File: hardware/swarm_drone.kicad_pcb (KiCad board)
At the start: 4 copper layers, 45 x 45 mm, 105 parts, among them J1 Conn_01x02_Pin, J2 Conn_01x03_Socket, J3 Conn_01x03_Socket, J5 Conn_01x02_Socket, J6 Conn_01x02_Socket, J7 Conn_01x02_Socket, J8 Conn_01x02_Socket, Q1 AO3400A, Q2 AO3400A, Q3 AO3400A, Q4 AO3400A, SW1 SW_Push, U1 STM32F405RGT7, U2 TPS7A91, U3 ICM-42688-P, U4 BMP581, U5 VL53L1CXV0FY1, U6 GD25Q128ESIGR, U7 nRF24L01P, X1 8MHz, Y1 16MHz (C13738)

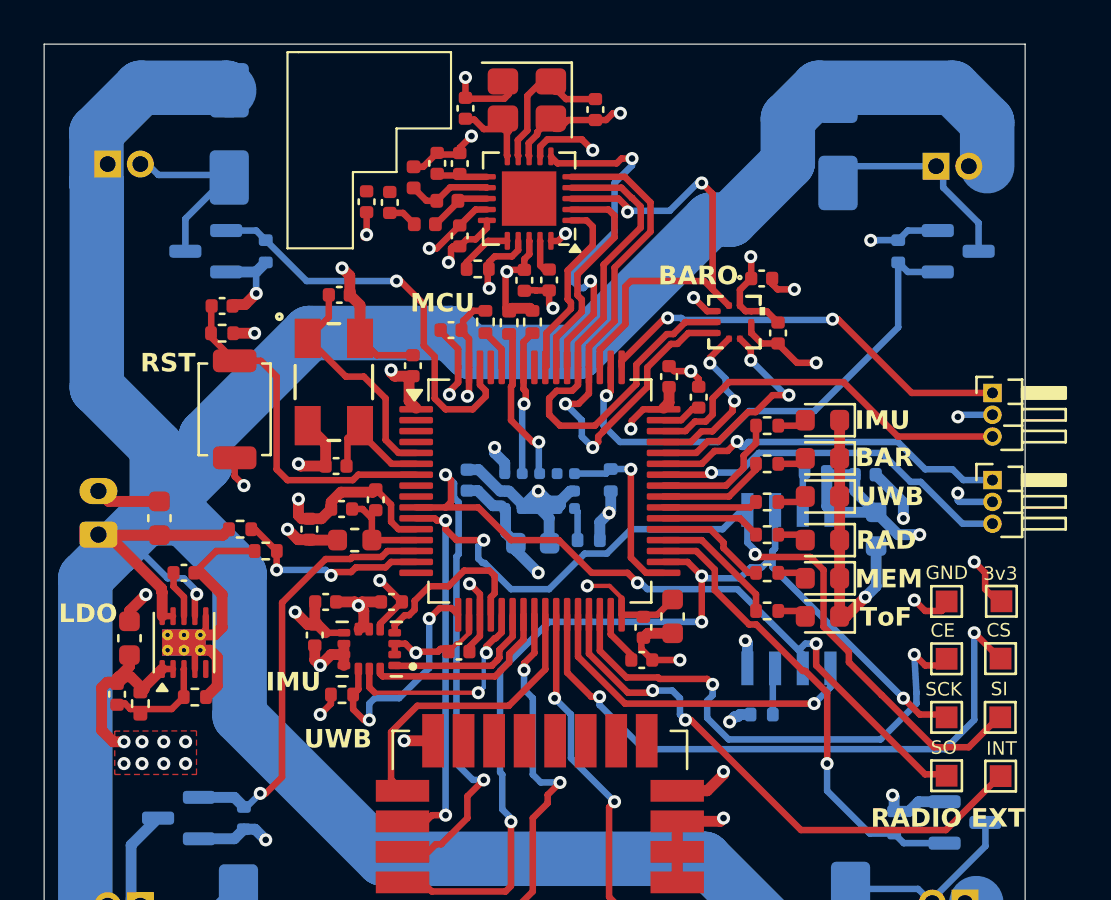
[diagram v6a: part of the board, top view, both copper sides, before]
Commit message: feat(kicad): Added chip antenna footprint Still deciding between chip vs trace
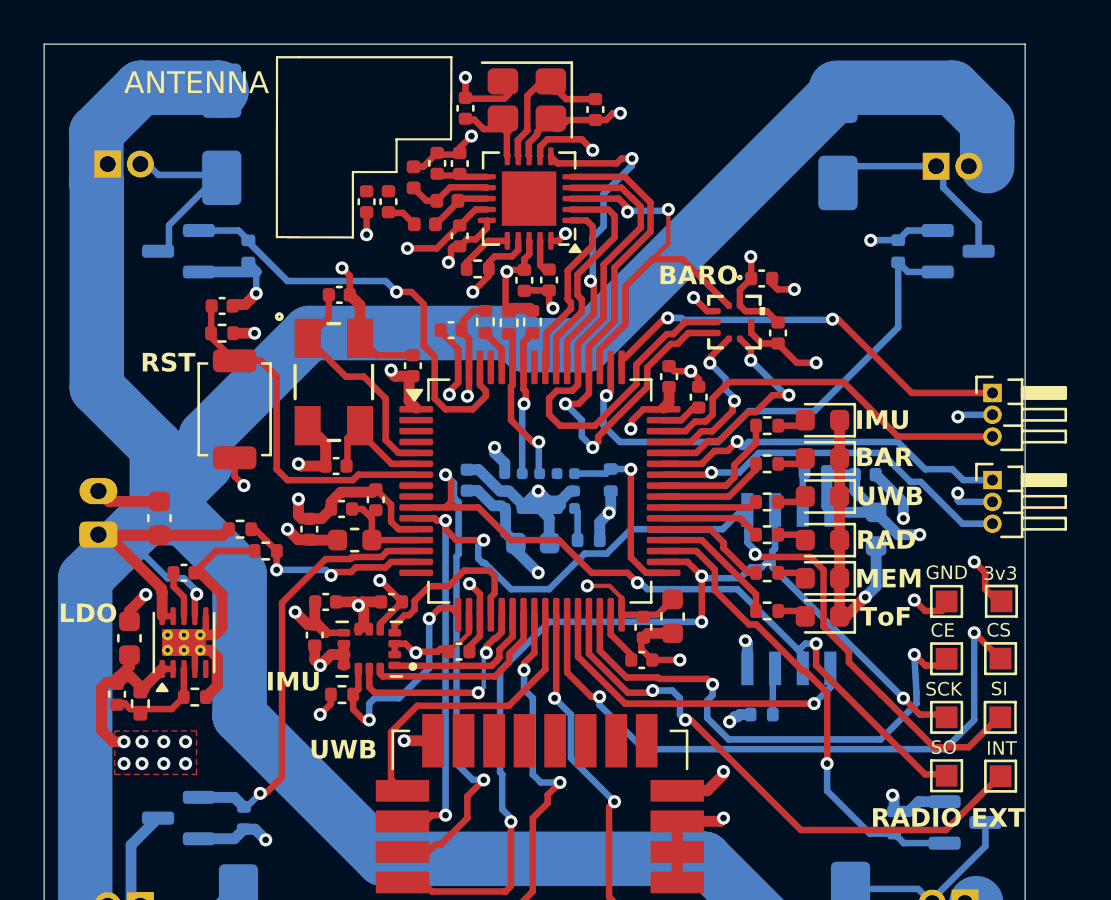
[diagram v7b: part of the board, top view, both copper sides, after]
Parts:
- moved Q1 1.25 mm to (84.5, 49.1)
- moved R12 0.80 mm to (87.7, 49.1)
- moved D1 0.34 mm to (86.5, 43.8)
- moved C33 0.07 mm to (94.1, 46.9)
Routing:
- net /Barometer/SPI3_SCK: track 21.5 -> 17.8 mm
- net GND: track 153.6 -> 155.7 mm
- net +BATT: track 177.0 -> 175.2 mm
- net /Microcontroller/RADIO_INT: track 16.3 -> 14.9 mm
- net /Microcontroller/M1: track 19.2 -> 20.0 mm
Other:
- board text added: "ANTENNA"
- board text removed: "MCU"

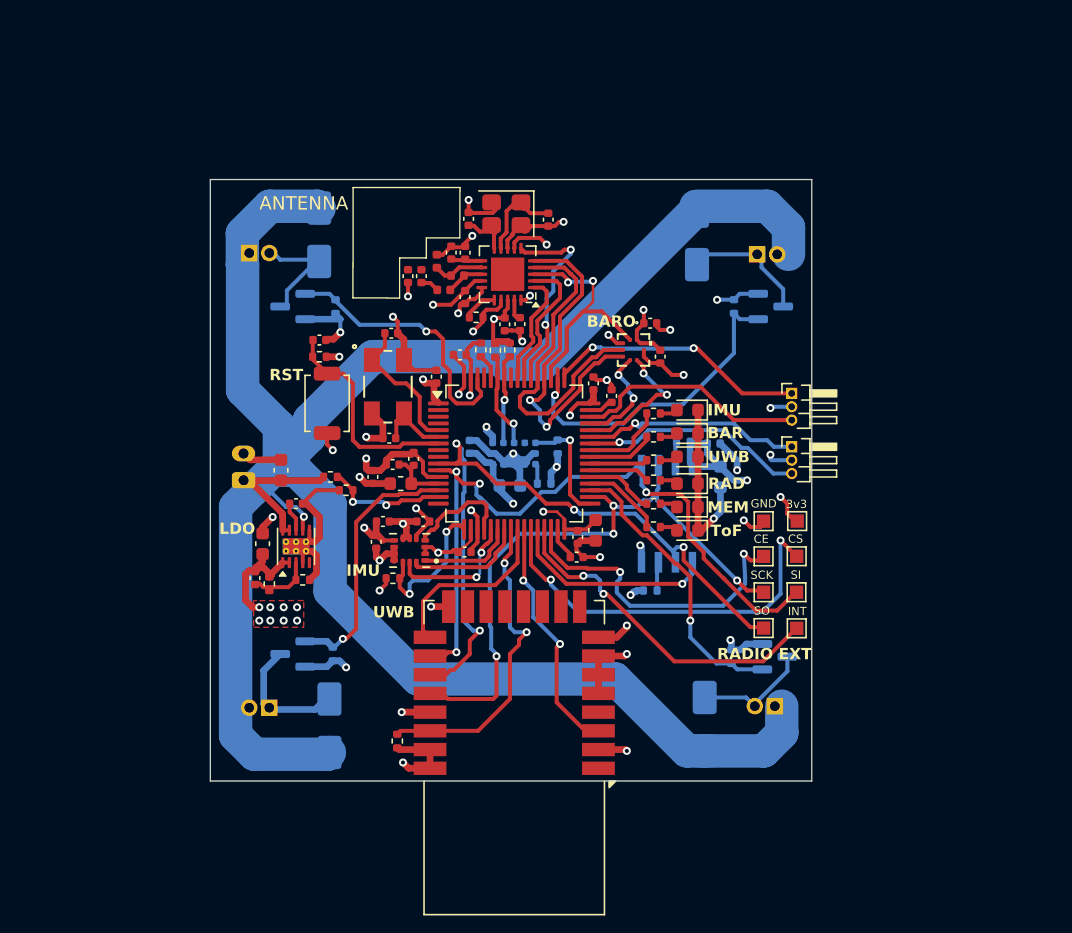
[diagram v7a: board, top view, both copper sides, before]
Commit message: feat(kicad): After several revisions finished rf section and improved ground plane topology and signal distances
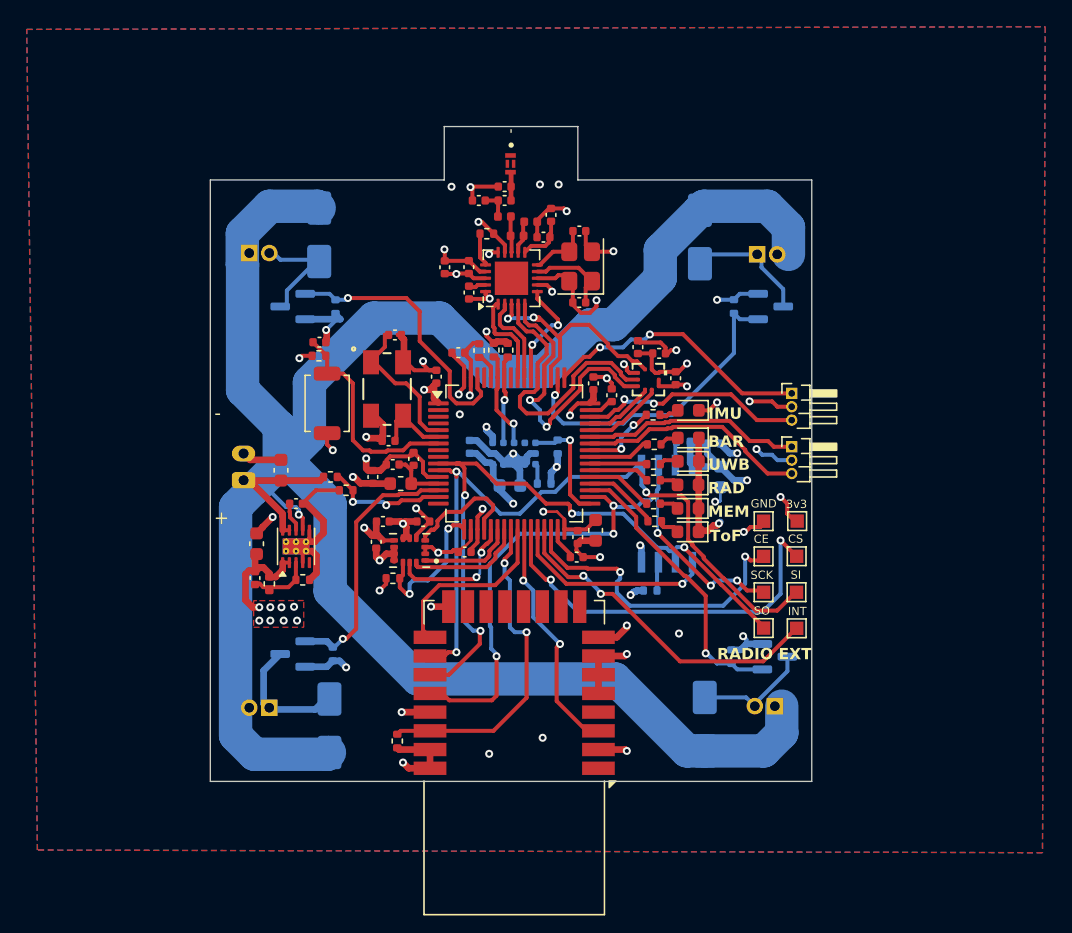
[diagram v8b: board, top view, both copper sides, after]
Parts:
- removed the C20 at (111.2, 50.4)
- added ANT1: ANT016008LCS2442MA1, Antenna:ANT_ANT016008LCS2442MA1, F.Cu at (100.8, 38.5)
- added C20: 100n, Capacitor_SMD:C_0402_1005Metric, F.Cu at (111.9, 52.6)
- added C20: 100n, Capacitor_SMD:C_0402_1005Metric, F.Cu at (110.3, 52.2)
- added C37: 1p, Capacitor_SMD:C_0402_1005Metric, F.Cu at (98.4, 41.2)
- moved C34 9.86 mm to (100.4, 40.2), turned to 0 degrees
- moved C33 8.41 mm to (100.4, 41.2), turned to 0 degrees
- moved C36 8.34 mm to (105.9, 43.5), turned to 0 degrees
- moved L1 7.62 mm to (102.3, 42.8), turned to 0 degrees
- moved L2 7.12 mm to (100.3, 42.4)
- moved C31 7.03 mm to (103.8, 42.3)
- moved C32 6.99 mm to (103.3, 43.9), turned to 180 degrees
- moved Y1 6.82 mm to (106.0, 46.1), turned to 90 degrees
- moved C35 6.62 mm to (105.9, 48.8), turned to 180 degrees
- moved R20 6.31 mm to (99.0, 43.7)
- moved C30 6.19 mm to (95.9, 46.2), turned to 90 degrees
- moved L3 5.36 mm to (101.3, 43.8), turned to 0 degrees
- moved C28 4.48 mm to (97.7, 48.1)
- moved U4 2.48 mm to (111.1, 54.6)
- moved C29 2.26 mm to (97.7, 46.2)
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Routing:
- net /Microcontroller/RADIO_INT: track 14.9 -> 8.19 mm
- net +BATT: track 175.2 -> 180.3 mm
- net GND: track 155.7 -> 160.4 mm, vias 38 -> 46
- net /Barometer/SPI3_MISO: track 26.5 -> 21.9 mm
- net /Barometer/BARO_INT: track 10.5 -> 6.03 mm, vias 2 -> 0
- net /Barometer/SPI3_MOSI: track 25.7 -> 21.8 mm
- net /Flash Memory/SPI2_MISO: track 53.7 -> 50.3 mm
- net /Microcontroller/RADIO_CS: track 10.3 -> 7.15 mm
- net /Barometer/BARO_CS: track 7.94 -> 5.24 mm, vias 2 -> 0
- net +3V3: track 84.1 -> 81.9 mm, vias 29 -> 30
- net /Radio/50ohm: track 0.00 -> 2.14 mm
- net /Flash Memory/SPI2_SCK: track 47.1 -> 49.2 mm, vias 4 -> 6
- net /Microcontroller/RADIO_CE: track 8.58 -> 7.18 mm
- net /Radio/ANT1: track 3.87 -> 2.51 mm
- net /Radio/VDD_PA: track 2.43 -> 3.75 mm
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- added copper zone on B.Cu, net GND
- added copper zone on F.Cu, net GND
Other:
- board size 45 x 45 mm -> 45 x 49 mm
- board text added: "+"
- board text added: "-"
- board text added: "RX"
- board text added: "SWCLK"
- board text added: "SWDIO"
- board text added: "TX"
- board text removed: "ANTENNA"
- board text removed: "BARO"
- board text removed: "LDO"
- board text removed: "RST"
